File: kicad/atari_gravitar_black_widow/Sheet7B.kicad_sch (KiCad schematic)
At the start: 37 parts, among them Q10 2N3904, Q5 2N3904, Q6 2N3904, Q7 2N3906, Q8 2N3904, Q9 2N3904

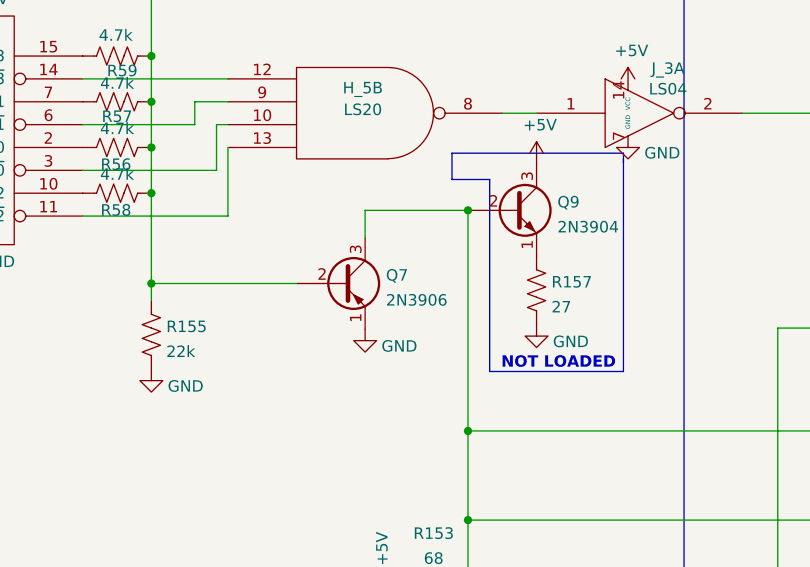
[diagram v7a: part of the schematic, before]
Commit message: more traces top left
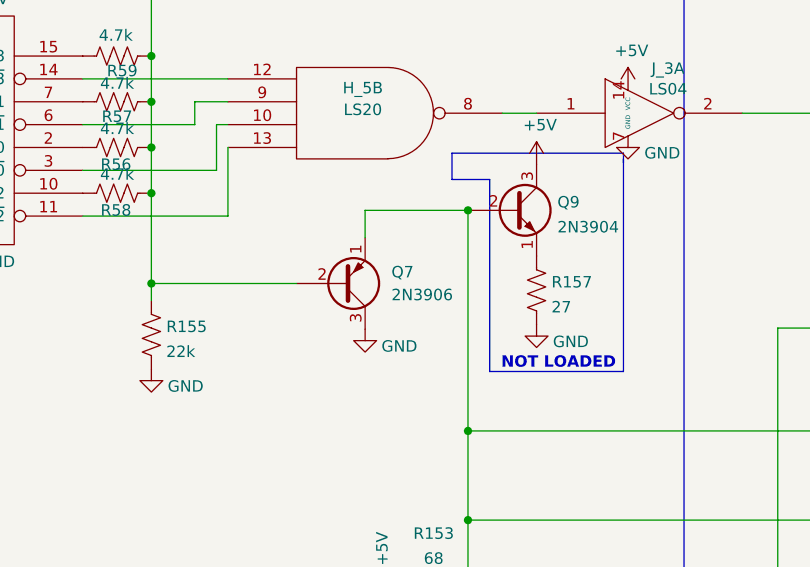
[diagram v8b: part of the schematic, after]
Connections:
- net GND: now also Q7.3 (C); no longer Q7.1 (E)
- net Z_OUT: now also Q7.1 (E); no longer Q7.3 (C)
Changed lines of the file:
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@@
     (pin "1")
   )
-  (symbol (lib_id "atari_gravitar_black_widow-rescue:2N3906-Star_Wars_Vector_PCB-rescue") (at 209.169 249.301 0) (unit 1)
+  (symbol (lib_id "atari_gravitar_black_widow-rescue:2N3906-Star_Wars_Vector_PCB-rescue") (at 209.169 249.301 0) (mirror x) (unit 1)
     (in_bom yes) (on_board yes) (fields_autoplaced)
-    (property "Reference" "Q7" (id 0) (at 214.0204 248.3925 0)
+    (property "Reference" "Q7" (id 0) (at 214.63 248.0309 0)
       (effects (font (size 1.27 1.27)) (justify left))
     )
-    (property "Value" "2N3906" (id 1) (at 214.0204 251.1676 0)
+    (property "Value" "2N3906" (id 1) (at 214.63 250.5709 0)
       (effects (font (size 1.27 1.27)) (justify left))
     )
-    (property "Footprint" "quantum_arcade_pcb:GenTrans" (id 2) (at 214.249 251.206 0)
+    (property "Footprint" "quantum_arcade_pcb:GenTrans" (id 2) (at 214.249 247.396 0)
       (effects (font (size 1.27 1.27) italic) (justify left) hide)
     )
